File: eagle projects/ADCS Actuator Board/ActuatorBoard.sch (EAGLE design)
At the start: 147 parts, among them J19 TE_1-84953-1, J20 TE_1-84953-1, J21 TE_1-84953-1, U1 TVS991, U10 DRV10970_MOTOR_DRIVERDRV10970, U12 DRV10970_MOTOR_DRIVERDRV10970, U2 ADS7841E_2K5, U3 ADS7841E_2K5, U35 BD6210F-E2, U39 BD6210F-E2, U5 TVS991, U7 DRV10970_MOTOR_DRIVERDRV10970, U8 TVS991, U9 BD6210F-E2

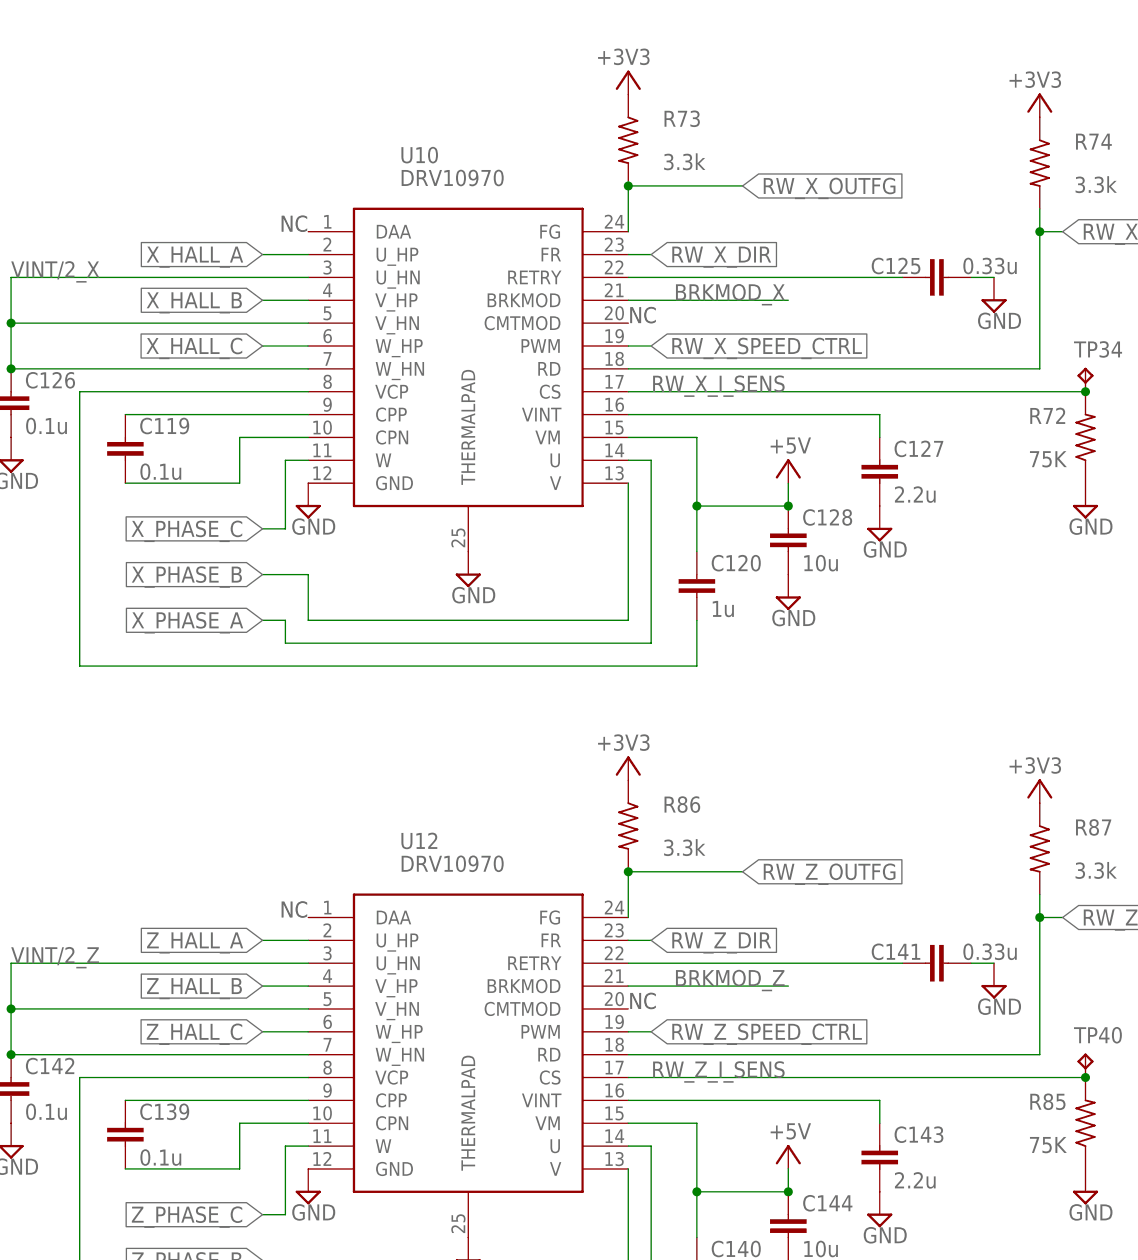
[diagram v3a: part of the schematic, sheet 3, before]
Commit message: tied floating pins on Actuator Board
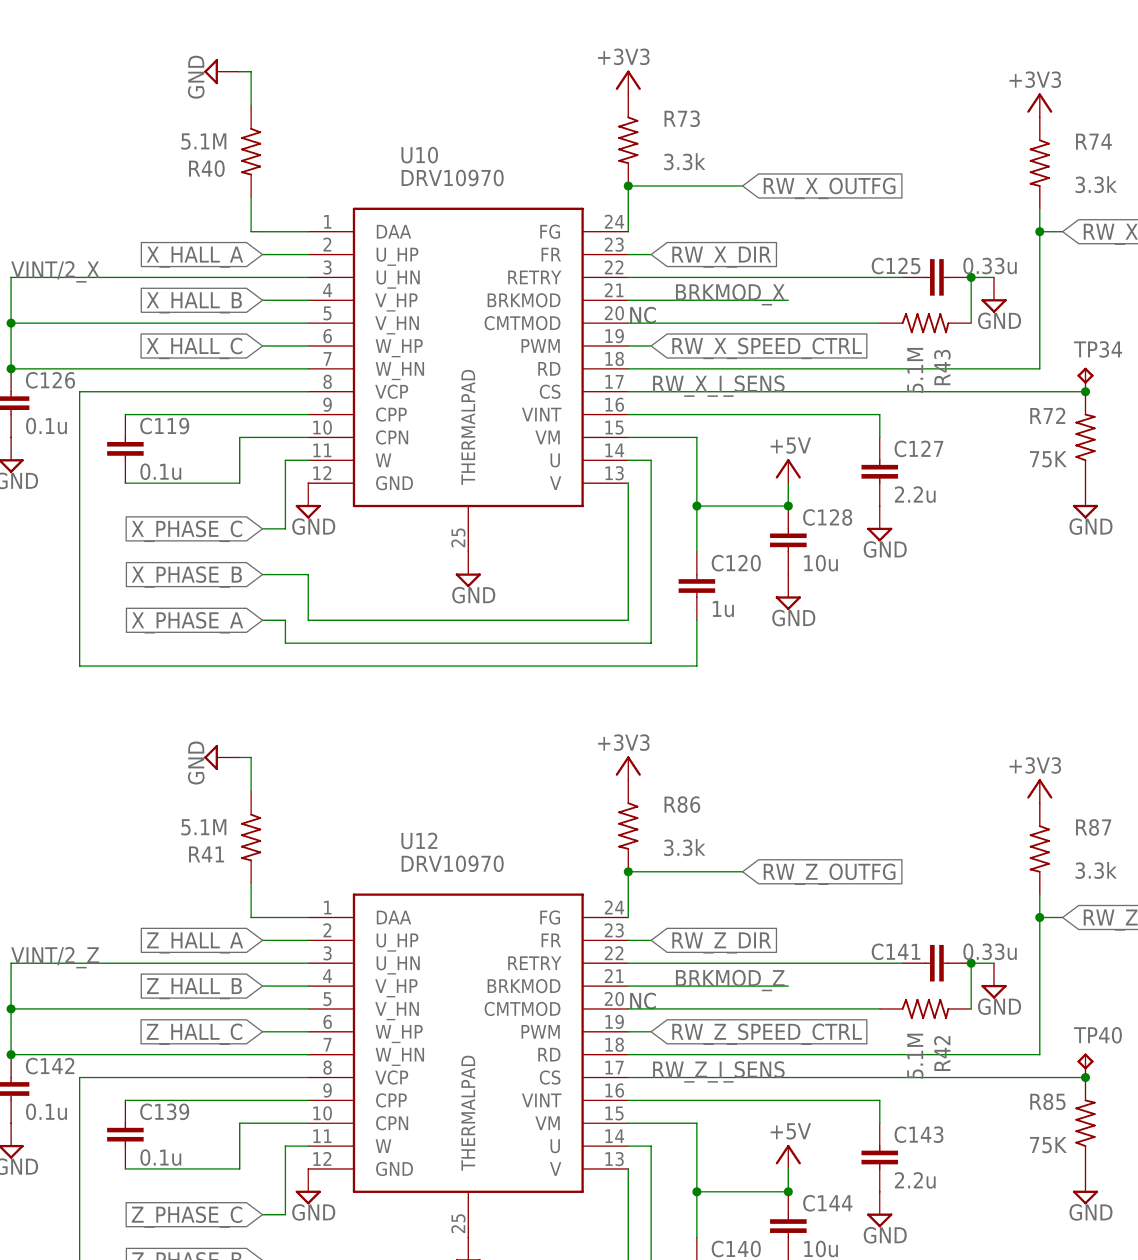
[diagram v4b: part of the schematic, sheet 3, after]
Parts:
- added R39, R40, R41, R42, R43, R44: 5.1M, rcl:R-US_R0402
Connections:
- new net N$19: R40.2, U10.DAA
- new net N$20: R41.2, U12.DAA
- new net N$22: R42.1, U12.CMTMOD
- new net N$23: R43.1, U10.CMTMOD
- new net N$24: R44.1, U7.CMTMOD
- new net N$3: R39.2, U7.DAA
- net GND: now also R39.1, R40.1, R41.1, R42.2, R43.2, R44.2
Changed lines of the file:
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@@
 <part name="R38" library="rcl" library_urn="urn:adsk.eagle:library:334" deviceset="R-US_" device="R0402" package3d_urn="urn:adsk.eagle:package:23547/3" value="1.8k"/>
 <part name="SUPPLY23" library="supply2" library_urn="urn:adsk.eagle:library:372" deviceset="GND" device=""/>
+<part name="R39" library="rcl" library_urn="urn:adsk.eagle:library:334" deviceset="R-US_" device="R0402" package3d_urn="urn:adsk.eagle:package:23547/3" value="5.1M"/>
+<part name="SUPPLY29" library="supply2" library_urn="urn:adsk.eagle:library:372" deviceset="GND" device=""/>
+<part name="R40" library="rcl" library_urn="urn:adsk.eagle:library:334" deviceset="R-US_" device="R0402" package3d_urn="urn:adsk.eagle:package:23547/3" value="5.1M"/>
+<part name="SUPPLY38" library="supply2" library_urn="urn:adsk.eagle:library:372" deviceset="GND" device=""/>
+<part name="R41" library="rcl" library_urn="urn:adsk.eagle:library:334" deviceset="R-US_" device="R0402" package3d_urn="urn:adsk.eagle:package:23547/3" value="5.1M"/>
+<part name="SUPPLY39" library="supply2" library_urn="urn:adsk.eagle:library:372" deviceset="GND" device=""/>
+<part name="R42" library="rcl" library_urn="urn:adsk.eagle:library:334" deviceset="R-US_" device="R0402" package3d_urn="urn:adsk.eagle:package:23547/3" value="5.1M"/>
+<part name="R43" library="rcl" library_urn="urn:adsk.eagle:library:334" deviceset="R-US_" device="R0402" package3d_urn="urn:adsk.eagle:package:23547/3" value="5.1M"/>
+<part name="R44" library="rcl" library_urn="urn:adsk.eagle:library:334" deviceset="R-US_" device="R0402" package3d_urn="urn:adsk.eagle:package:23547/3" value="5.1M"/>
 </parts>
 <sheets>
@@
 VCP: Connect a 16V 1-uF cap to VM
 CS: Connect a resistor to adhjust the current limit</text>
-<text x="88.9" y="177.8" size="1.778" layer="97" rot="MR0">NC</text>
 <text x="124.46" y="167.64" size="1.778" layer="97">NC</text>
-<text x="88.9" y="101.6" size="1.778" layer="97" rot="MR0">NC</text>
 <text x="124.46" y="91.44" size="1.778" layer="97">NC</text>
 <text x="71.12" y="15.24" size="1.778" layer="97">DAA: Drive angle adjustment configuration pin
@@
 <attribute name="VALUE" x="38.735" y="179.705" size="1.778" layer="96"/>
 </instance>
+<instance part="R40" gate="G$1" x="82.55" y="186.69" smashed="yes" rot="R270">
+<attribute name="NAME" x="79.756" y="185.6994" size="1.778" layer="95" rot="R180"/>
+<attribute name="VALUE" x="80.01" y="188.722" size="1.778" layer="96" rot="R180"/>
+</instance>
+<instance part="SUPPLY38" gate="GND" x="78.74" y="195.58" smashed="yes" rot="R270">
+<attribute name="VALUE" x="75.565" y="197.485" size="1.778" layer="96" rot="R270"/>
+</instance>
+<instance part="R41" gate="G$1" x="82.55" y="110.49" smashed="yes" rot="R270">
+<attribute name="NAME" x="79.756" y="109.4994" size="1.778" layer="95" rot="R180"/>
+<attribute name="VALUE" x="80.01" y="112.522" size="1.778" layer="96" rot="R180"/>
+</instance>
+<instance part="SUPPLY39" gate="GND" x="78.74" y="119.38" smashed="yes" rot="R270">
+<attribute name="VALUE" x="75.565" y="121.285" size="1.778" layer="96" rot="R270"/>
+</instance>
+<instance part="R42" gate="G$1" x="157.48" y="91.44" smashed="yes">
+<attribute name="NAME" x="158.4706" y="88.646" size="1.778" layer="95" rot="R270"/>
+<attribute name="VALUE" x="155.448" y="88.9" size="1.778" layer="96" rot="R270"/>
+</instance>
+<instance part="R43" gate="G$1" x="157.48" y="167.64" smashed="yes">
+<attribute name="NAME" x="158.4706" y="164.846" size="1.778" layer="95" rot="R270"/>
+<attribute name="VALUE" x="155.448" y="165.1" size="1.778" layer="96" rot="R270"/>
+</instance>
 </instances>
 <busses>
@@
 <pinref part="C125" gate="G$1" pin="2"/>
 <wire x1="162.56" y1="172.72" x2="165.1" y2="172.72" width="0.1524" layer="91"/>
+<pinref part="R43" gate="G$1" pin="2"/>
+<wire x1="162.56" y1="167.64" x2="162.56" y2="172.72" width="0.1524" layer="91"/>
+<junction x="162.56" y="172.72"/>
 </segment>
 <segment>
@@
 <pinref part="C141" gate="G$1" pin="2"/>
 <wire x1="162.56" y1="96.52" x2="165.1" y2="96.52" width="0.1524" layer="91"/>
+<pinref part="R42" gate="G$1" pin="2"/>
+<wire x1="162.56" y1="91.44" x2="162.56" y2="96.52" width="0.1524" layer="91"/>
+<junction x="162.56" y="96.52"/>
 </segment>
 <segment>
@@
 <pinref part="SUPPLY11" gate="GND" pin="GND"/>
 </segment>
+<segment>
+<pinref part="R40" gate="G$1" pin="1"/>
+<pinref part="SUPPLY38" gate="GND" pin="GND"/>
+<wire x1="82.55" y1="191.77" x2="82.55" y2="195.58" width="0.1524" layer="91"/>
+<wire x1="82.55" y1="195.58" x2="81.28" y2="195.58" width="0.1524" layer="91"/>
+</segment>
+<segment>
+<pinref part="R41" gate="G$1" pin="1"/>
+<pinref part="SUPPLY39" gate="GND" pin="GND"/>
+<wire x1="82.55" y1="115.57" x2="82.55" y2="119.38" width="0.1524" layer="91"/>
+<wire x1="82.55" y1="119.38" x2="81.28" y2="119.38" width="0.1524" layer="91"/>
+</segment>
 </net>
 <net name="+5V" class="0">
@@
 </segment>
 </net>
+<net name="N$19" class="0">
+<segment>
+<pinref part="U10" gate="G$1" pin="DAA"/>
+<wire x1="88.9" y1="177.8" x2="83.82" y2="177.8" width="0.1524" layer="91"/>
+<pinref part="R40" gate="G$1" pin="2"/>
+<wire x1="83.82" y1="177.8" x2="82.55" y2="177.8" width="0.1524" layer="91"/>
+<wire x1="82.55" y1="177.8" x2="82.55" y2="181.61" width="0.1524" layer="91"/>
+</segment>
+</net>
+<net name="N$20" class="0">
+<segment>
+<pinref part="U12" gate="G$1" pin="DAA"/>
+<pinref part="R41" gate="G$1" pin="2"/>
+<wire x1="82.55" y1="105.41" x2="82.55" y2="101.6" width="0.1524" layer="91"/>
+<wire x1="82.55" y1="101.6" x2="88.9" y2="101.6" width="0.1524" layer="91"/>
+</segment>
+</net>
+<net name="N$22" class="0">
+<segment>
+<pinref part="U12" gate="G$1" pin="CMTMOD"/>
+<pinref part="R42" gate="G$1" pin="1"/>
+<wire x1="124.46" y1="91.44" x2="152.4" y2="91.44" width="0.1524" layer="91"/>
+</segment>
+</net>
+<net name="N$23" class="0">
+<segment>
+<pinref part="U10" gate="G$1" pin="CMTMOD"/>
+<pinref part="R43" gate="G$1" pin="1"/>
+<wire x1="124.46" y1="167.64" x2="152.4" y2="167.64" width="0.1524" layer="91"/>
+</segment>
+</net>
 </nets>
 </sheet>
@@
 <attribute name="VALUE" x="191.77" y="94.488" size="1.778" layer="96"/>
 </instance>
+<instance part="R39" gate="G$1" x="67.31" y="72.39" smashed="yes" rot="R270">
+<attribute name="NAME" x="64.516" y="71.3994" size="1.778" layer="95" rot="R180"/>
+<attribute name="VALUE" x="64.77" y="74.422" size="1.778" layer="96" rot="R180"/>
+</instance>
+<instance part="SUPPLY29" gate="GND" x="63.5" y="81.28" smashed="yes" rot="R270">
+<attribute name="VALUE" x="60.325" y="83.185" size="1.778" layer="96" rot="R270"/>
+</instance>
+<instance part="R44" gate="G$1" x="144.78" y="53.34" smashed="yes">
+<attribute name="NAME" x="145.7706" y="50.546" size="1.778" layer="95" rot="R270"/>
+<attribute name="VALUE" x="142.748" y="50.8" size="1.778" layer="96" rot="R270"/>
+</instance>
 </instances>
 <busses>
@@
 <pinref part="C15" gate="G$1" pin="2"/>
 <wire x1="149.86" y1="58.42" x2="152.4" y2="58.42" width="0.1524" layer="91"/>
+<pinref part="R44" gate="G$1" pin="2"/>
+<wire x1="149.86" y1="53.34" x2="149.86" y2="58.42" width="0.1524" layer="91"/>
+<junction x="149.86" y="58.42"/>
 </segment>
 <segment>
@@
 <pinref part="J6" gate="A" pin="1"/>
 </segment>
+<segment>
+<pinref part="R39" gate="G$1" pin="1"/>
+<pinref part="SUPPLY29" gate="GND" pin="GND"/>
+<wire x1="67.31" y1="77.47" x2="67.31" y2="81.28" width="0.1524" layer="91"/>
+<wire x1="67.31" y1="81.28" x2="66.04" y2="81.28" width="0.1524" layer="91"/>
+</segment>
 </net>
 <net name="Z_HALL_B" class="0">
@@
 </segment>
 </net>
+<net name="N$3" class="0">
+<segment>
+<pinref part="U7" gate="G$1" pin="DAA"/>
+<pinref part="R39" gate="G$1" pin="2"/>
+<wire x1="76.2" y1="63.5" x2="67.31" y2="63.5" width="0.1524" layer="91"/>
+<wire x1="67.31" y1="63.5" x2="67.31" y2="67.31" width="0.1524" layer="91"/>
+</segment>
+</net>
+<net name="N$24" class="0">
+<segment>
+<pinref part="R44" gate="G$1" pin="1"/>
+<pinref part="U7" gate="G$1" pin="CMTMOD"/>
+<wire x1="139.7" y1="53.34" x2="111.76" y2="53.34" width="0.1524" layer="91"/>
+</segment>
+</net>

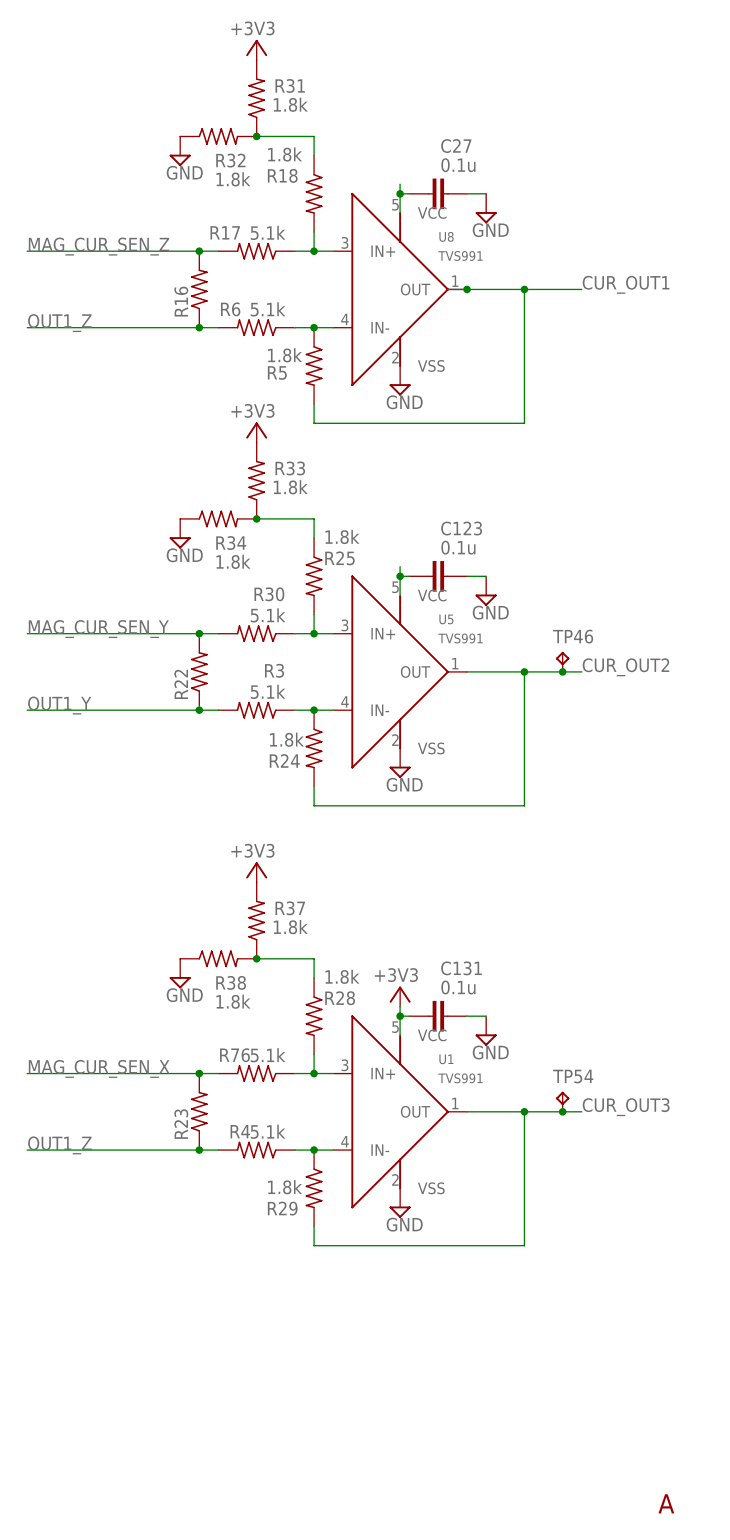
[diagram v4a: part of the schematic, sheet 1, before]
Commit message: Added missing power supplies to magnetorquer current senses
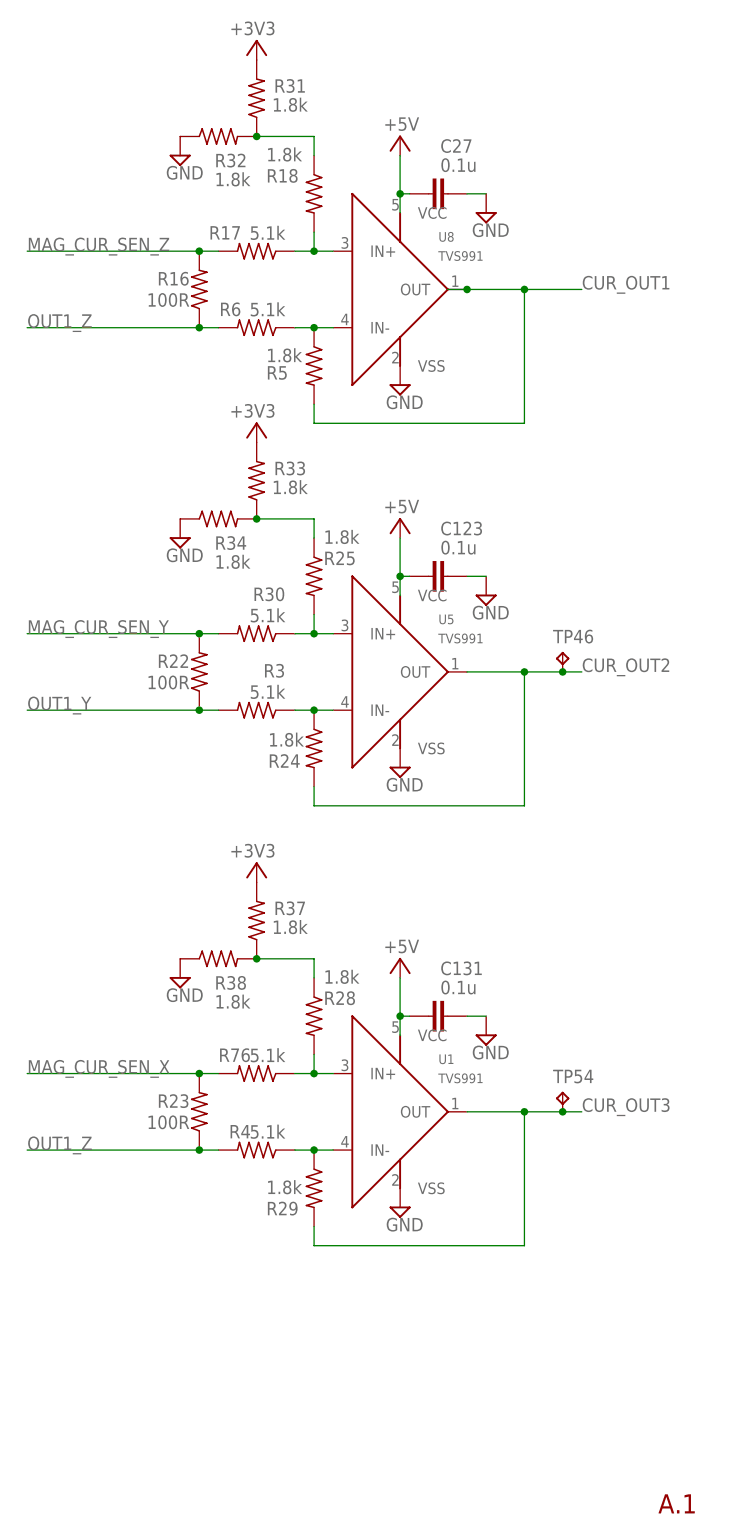
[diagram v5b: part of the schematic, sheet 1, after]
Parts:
- R16, R22, R23: value (none) -> 100R
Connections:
- removed net N$1: C123.1, U5.VCC
- removed net N$2: C27.1, U8.VCC
- net +3V3: no longer C131.1, U1.VCC
- net +5V: now also C123.1, C131.1, C27.1, U1.VCC, U5.VCC, U8.VCC
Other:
- note added: "A.1"
- note removed: "A"
